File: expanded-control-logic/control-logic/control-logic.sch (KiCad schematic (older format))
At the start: 43 parts

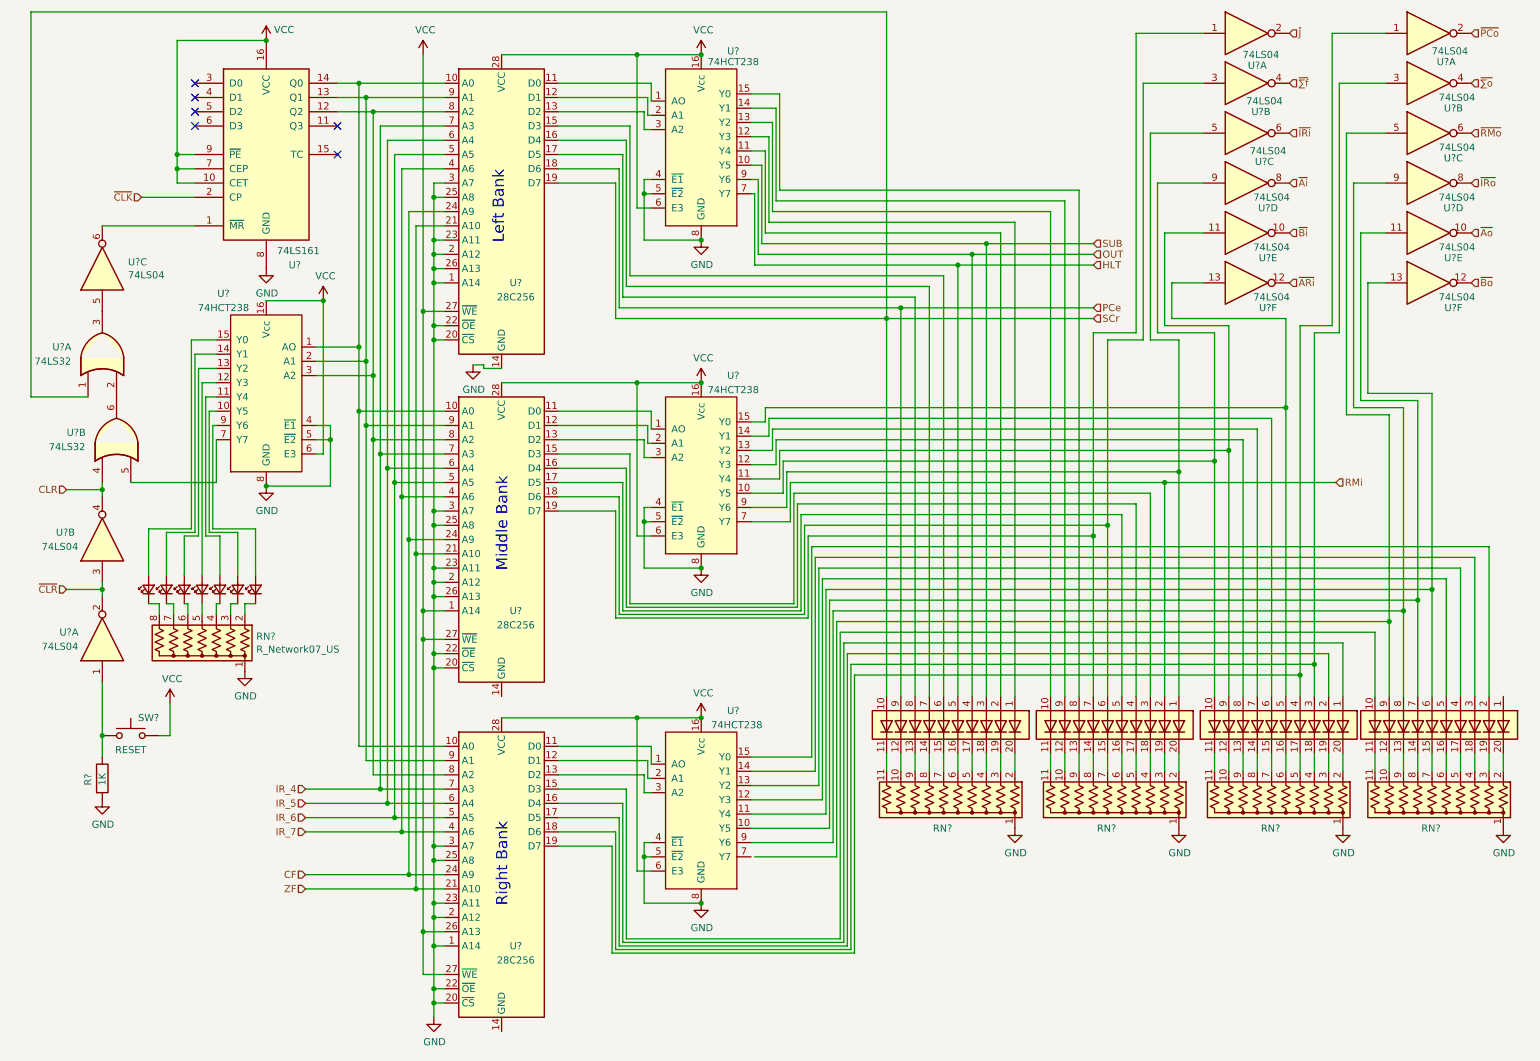
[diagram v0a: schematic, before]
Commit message: fixed werror where Y0 on 74HCT238 cannot be used for control lines
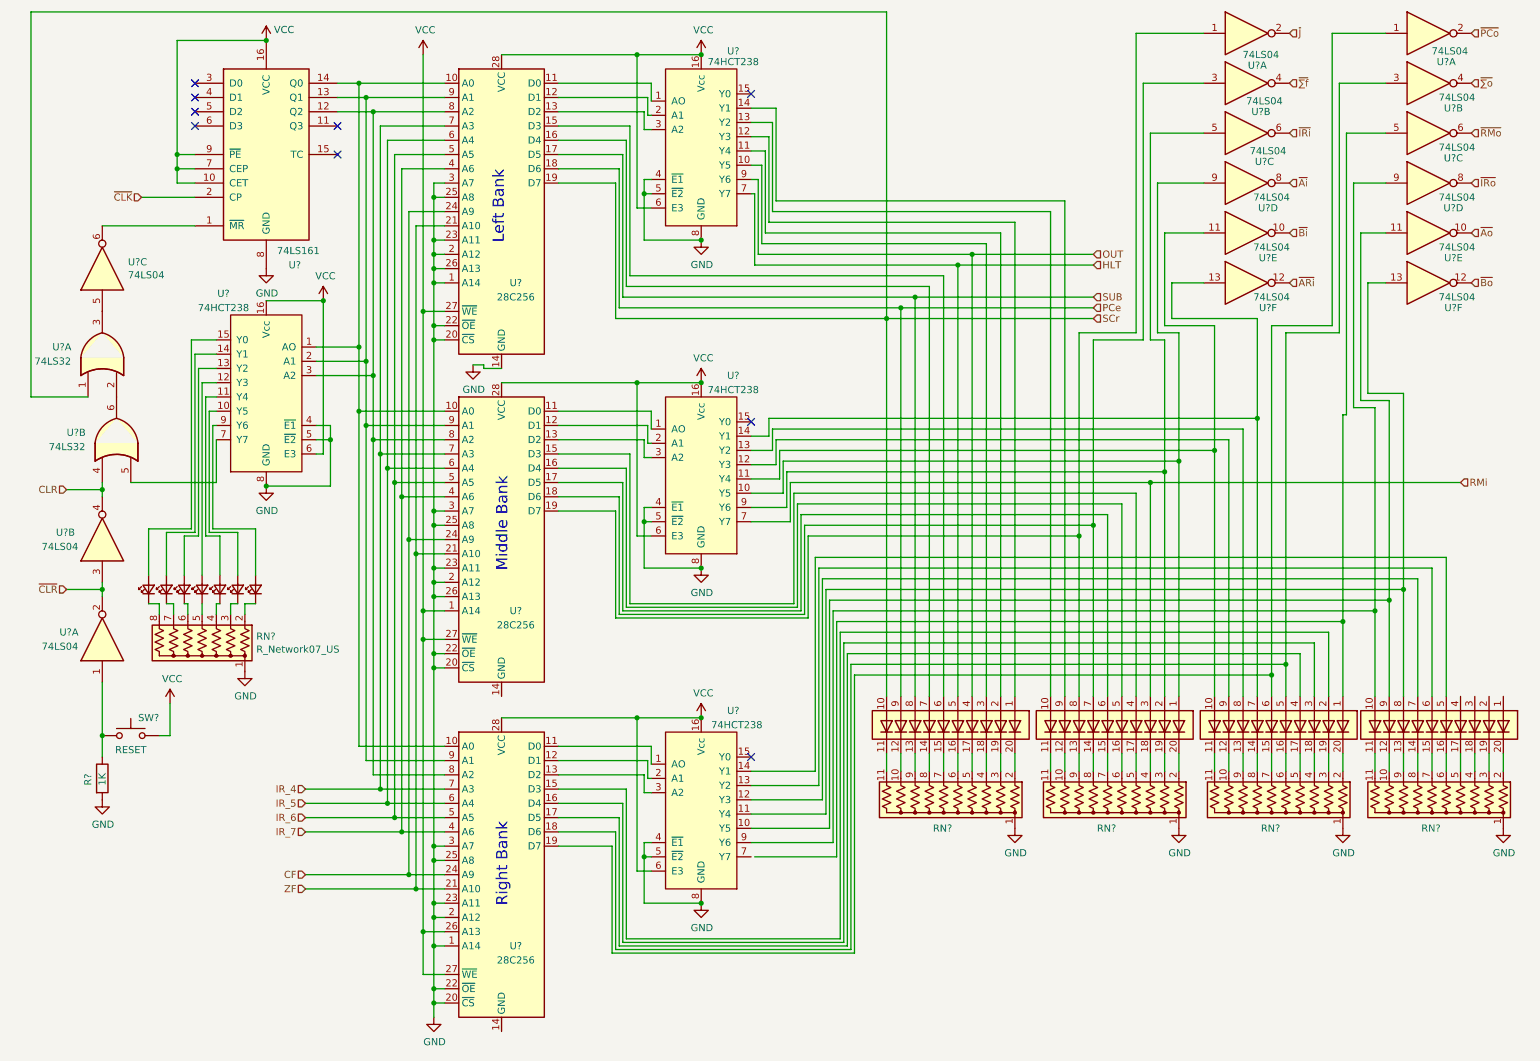
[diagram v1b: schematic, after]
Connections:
- net RMi: now also BAR?.3 (A); no longer BAR?.2 (A)
- net SUB: now also BAR?.8 (A), U?.17 (D5); no longer BAR?.3 (A), U?.10 (Y5)
- net at U?.15 (D3): now also BAR?.4 (A); no longer BAR?.3 (A)
- net at U?.16 (D4): now also BAR?.5 (A); no longer BAR?.4 (A)
- net at U?.17 (D5): now also BAR?.6 (A); no longer BAR?.5 (A)
- net at U?.18 (D6), U?.3: now also BAR?.7 (A); no longer BAR?.6 (A)
- net at U?.1, U?.19 (D7): now also BAR?.8 (A); no longer BAR?.7 (A)
- net at U?.15 (D3): now also BAR?.2 (A); no longer BAR?.10 (A)
- net at U?.16 (D4): now also BAR?.3 (A); no longer BAR?.1 (A)
- net at U?.17 (D5): now also BAR?.4 (A); no longer BAR?.2 (A)
- net at U?.18 (D6), U?.3: now also BAR?.5 (A); no longer BAR?.3 (A)
- net at U?.1, U?.19 (D7): now also BAR?.6 (A); no longer BAR?.4 (A)
- net at U?.15 (Y0): no longer BAR?.8 (A)
- net at U?.10 (Y5), U?.9: now also BAR?.1 (A); no longer BAR?.10 (A)
- net at U?.11, U?.11 (Y4): now also BAR?.10 (A); no longer BAR?.9 (A)
- net at U?.12 (Y3): now also BAR?.9 (A); no longer BAR?.8 (A)
- net at U?.13 (Y2): now also BAR?.8 (A); no longer BAR?.7 (A)
- net at U?.14 (Y1): now also BAR?.7 (A), U?.13; no longer BAR?.6 (A)
- net at U?.5, U?.9 (Y6): now also BAR?.2 (A); no longer BAR?.1 (A)
- net at U?.10 (Y5), U?.11: now also BAR?.9 (A); no longer BAR?.7 (A)
- net at U?.11 (Y4), U?.13: now also BAR?.8 (A); no longer BAR?.6 (A)
- net at U?.12 (Y3): now also BAR?.7 (A); no longer BAR?.5 (A)
- net at U?.13 (Y2): now also BAR?.6 (A); no longer BAR?.4 (A)
- net at U?.14 (Y1): now also BAR?.5 (A); no longer BAR?.3 (A)
- net at U?.15 (Y0): no longer BAR?.2 (A)
- net at U?.9, U?.9 (Y6): now also BAR?.10 (A); no longer BAR?.8 (A)
- net at U?.5: now also BAR?.1 (A); no longer BAR?.9 (A)
- new net: BAR?.3 (A), U?.10 (Y5)
- now unconnected: U?.15 (Y0)
- no-connect marks 6 -> 9
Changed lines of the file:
@@
 Text HLabel 10625 1025 2    50   Input ~ 0
 ~∑o
-Text HLabel 7975 2150 2    50   Input ~ 0
+Text HLabel 7975 2525 2    50   Input ~ 0
 SUB
 Text HLabel 9350 2075 2    50   Input ~ 0
@@
 	4225 1725 4625 1725
 Wire Wire Line
-	5575 3400 5675 3400
-Wire Wire Line
 	5575 3500 5700 3500
 Wire Wire Line
@@
 	4625 4775 5975 4775
 Wire Wire Line
-	5575 5750 6000 5750
-Wire Wire Line
 	5575 5850 6025 5850
 Wire Wire Line
@@
 Wire Wire Line
 	5575 1200 5750 1200
-Wire Wire Line
-	5575 1100 5775 1100
 $Comp
 L LED:HDSP-4840_2 BAR?
@@
 	5750 1200 5750 1850
 Wire Wire Line
-	5775 1775 7875 1775
-Wire Wire Line
-	7875 1775 7875 5325
-Wire Wire Line
-	5775 1100 5775 1775
-Wire Wire Line
-	5675 3400 5675 3300
-Wire Wire Line
 	5725 3600 5725 3450
 Wire Wire Line
@@
 	5975 4775 5975 4200
 Wire Wire Line
-	6000 5750 6000 4275
-Wire Wire Line
 	6025 5850 6025 4350
 Wire Wire Line
-	10750 5325 10750 4275
-Wire Wire Line
 	6050 5950 6050 4425
 Wire Wire Line
@@
 	6300 7125 6300 5175
 Wire Wire Line
-	6300 5175 9425 5175
-Wire Wire Line
-	9425 5175 9425 5325
-Wire Wire Line
-	9525 5100 6275 5100
-Wire Wire Line
-	9525 5100 9525 5325
+	6300 5175 9225 5175
 Wire Wire Line
 	6275 5100 6275 7100
 Wire Wire Line
-	9625 5025 6250 5025
-Wire Wire Line
-	9625 5025 9625 5325
-Wire Wire Line
 	6250 5025 6250 7075
 Wire Wire Line
-	9725 4950 6225 4950
-Wire Wire Line
-	9725 4950 9725 5325
-Wire Wire Line
-	9950 4875 6200 4875
-Wire Wire Line
-	9950 4875 9950 5325
-Wire Wire Line
-	10050 4800 6175 4800
-Wire Wire Line
-	10050 4800 10050 5325
-Wire Wire Line
-	10150 4725 6150 4725
-Wire Wire Line
-	10150 4725 10150 5325
-Wire Wire Line
-	10250 4650 6125 4650
-Wire Wire Line
-	10250 4650 10250 5325
-Wire Wire Line
-	10350 4575 6100 4575
-Wire Wire Line
-	10350 4575 10350 5325
-Wire Wire Line
-	10450 4500 6075 4500
-Wire Wire Line
-	10450 4500 10450 5325
-Wire Wire Line
-	10550 4425 6050 4425
-Wire Wire Line
-	10550 4425 10550 5325
-Wire Wire Line
-	10650 4350 6025 4350
-Wire Wire Line
-	10650 4350 10650 5325
-Wire Wire Line
-	10750 4275 6000 4275
-Wire Wire Line
-	7975 4200 5975 4200
-Wire Wire Line
-	7975 4200 7975 5325
-Wire Wire Line
-	5950 4125 8075 4125
-Wire Wire Line
-	8075 4125 8075 5325
-Wire Wire Line
-	8175 4050 5925 4050
-Wire Wire Line
-	8175 4050 8175 5325
-Wire Wire Line
-	8275 3975 5900 3975
-Wire Wire Line
-	8275 3975 8275 5325
-Wire Wire Line
-	8375 3900 5875 3900
-Wire Wire Line
-	8375 3900 8375 5325
-Wire Wire Line
-	8475 3825 5850 3825
-Wire Wire Line
-	8475 3825 8475 5325
-Wire Wire Line
-	8575 3750 5825 3750
-Wire Wire Line
-	8575 3750 8575 5325
-Wire Wire Line
-	8825 3675 5800 3675
-Wire Wire Line
-	8825 3675 8825 5325
-Wire Wire Line
-	8925 3600 5775 3600
-Wire Wire Line
-	8925 3600 8925 5325
-Wire Wire Line
-	9025 3525 5750 3525
-Wire Wire Line
-	9025 3525 9025 5325
-Wire Wire Line
-	9125 3450 5725 3450
-Wire Wire Line
-	9125 3450 9125 5325
-Wire Wire Line
-	9225 3375 5700 3375
-Wire Wire Line
-	9225 3375 9225 5325
+	5950 4125 7975 4125
 Wire Wire Line
 	5700 3375 5700 3500
-Wire Wire Line
-	9325 3300 5675 3300
-Wire Wire Line
-	9325 3300 9325 5325
 Wire Wire Line
 	6525 2675 6525 525
@@
 Connection ~ 7125 2225
 Wire Wire Line
-	7225 2150 7975 2150
-Connection ~ 7225 2150
-Wire Wire Line
 	6525 2675 7975 2675
 Wire Wire Line
-	7975 4200 7975 2775
-Wire Wire Line
-	7975 2775 8275 2775
-Wire Wire Line
 	8275 2775 8275 675
 Wire Wire Line
 	8275 675  8750 675
-Connection ~ 7975 4200
-Wire Wire Line
-	8075 4125 8075 2825
-Wire Wire Line
-	8075 2825 8325 2825
 Wire Wire Line
 	8325 2825 8325 1025
 Wire Wire Line
 	8325 1025 8750 1025
-Connection ~ 8075 4125
-Wire Wire Line
-	9425 5175 9425 2725
-Wire Wire Line
-	9425 2725 9650 2725
-Connection ~ 9425 5175
-Wire Wire Line
-	9525 5100 9525 2775
-Wire Wire Line
-	9525 2775 9700 2775
-Connection ~ 9525 5100
 $Comp
 L 74xx:74LS04 U?
@@
 	1    0    0    -1
 $EndComp
-Text HLabel 9675 3825 2    50   Input ~ 0
+Text HLabel 10550 3825 2    50   Input ~ 0
 RMi
 Wire Wire Line
-	8475 3825 9675 3825
-Connection ~ 8475 3825
-Wire Wire Line
-	8575 3750 8575 2825
-Wire Wire Line
-	8575 2825 8375 2825
-Wire Wire Line
 	8375 2825 8375 1375
 Wire Wire Line
 	8375 1375 8750 1375
-Connection ~ 8575 3750
-Wire Wire Line
-	8825 3675 8825 2775
-Wire Wire Line
-	8825 2775 8425 2775
 Wire Wire Line
 	8425 2775 8425 1725
 Wire Wire Line
 	8425 1725 8750 1725
-Connection ~ 8825 3675
-Wire Wire Line
-	8925 3600 8925 2725
-Wire Wire Line
-	8925 2725 8475 2725
 Wire Wire Line
 	8475 2725 8475 2075
 Wire Wire Line
 	8475 2075 8750 2075
-Connection ~ 8925 3600
-Wire Wire Line
-	9325 3300 9325 2675
-Wire Wire Line
-	9325 2675 8525 2675
 Wire Wire Line
 	8525 2675 8525 2425
 Wire Wire Line
 	8525 2425 8750 2425
-Connection ~ 9325 3300
 Wire Wire Line
 	9650 675  10025 675
@@
 	9700 1025 9700 2775
 Wire Wire Line
-	10050 4800 10050 3350
-Wire Wire Line
-	10050 3350 9750 3350
-Wire Wire Line
 	9750 3350 9750 1375
 Wire Wire Line
 	9750 1375 10025 1375
-Connection ~ 10050 4800
-Wire Wire Line
-	10150 4725 10150 3300
-Wire Wire Line
-	10150 3300 9800 3300
 Wire Wire Line
 	9800 3300 9800 1725
 Wire Wire Line
 	9800 1725 10025 1725
-Connection ~ 10150 4725
-Wire Wire Line
-	10250 4650 10250 3250
-Wire Wire Line
-	10250 3250 9850 3250
 Wire Wire Line
 	9850 3250 9850 2075
 Wire Wire Line
 	9850 2075 10025 2075
-Connection ~ 10250 4650
-Wire Wire Line
-	10350 4575 10350 3200
-Wire Wire Line
-	10350 3200 9900 3200
 Wire Wire Line
 	9900 3200 9900 2425
 Wire Wire Line
 	9900 2425 10025 2425
-Connection ~ 10350 4575
+Wire Wire Line
+	6725 2525 7975 2525
+Connection ~ 6725 2525
+NoConn ~ 5575 1100
+NoConn ~ 5575 3400
+NoConn ~ 5575 5750
+Wire Wire Line
+	7875 5325 7875 4200
+Wire Wire Line
+	7875 4200 5975 4200
+Wire Wire Line
+	7875 4200 7875 2775
+Wire Wire Line
+	7875 2775 8275 2775
+Connection ~ 7875 4200
+Wire Wire Line
+	7975 5325 7975 4125
+Wire Wire Line
+	7975 4125 7975 2825
+Wire Wire Line
+	7975 2825 8325 2825
+Connection ~ 7975 4125
+Wire Wire Line
+	8075 5325 8075 4050
+Wire Wire Line
+	8075 4050 5925 4050
+Wire Wire Line
+	8175 5325 8175 3975
+Wire Wire Line
+	8175 3975 5900 3975
+Wire Wire Line
+	8275 5325 8275 3900
+Wire Wire Line
+	8275 3900 5875 3900
+Wire Wire Line
+	5850 3825 8375 3825
+Wire Wire Line
+	8375 5325 8375 3825
+Wire Wire Line
+	8475 5325 8475 3750
+Connection ~ 8475 3750
+Wire Wire Line
+	8475 3750 5825 3750
+Wire Wire Line
+	8475 3750 8475 2825
+Wire Wire Line
+	8475 2825 8375 2825
+Wire Wire Line
+	8575 5325 8575 3675
+Wire Wire Line
+	8575 3675 5800 3675
+Wire Wire Line
+	8575 2775 8425 2775
+Wire Wire Line
+	8575 2775 8575 3675
+Connection ~ 8575 3675
+Wire Wire Line
+	8825 5325 8825 3600
+Connection ~ 8825 3600
+Wire Wire Line
+	8825 3600 5775 3600
+Wire Wire Line
+	8825 3600 8825 2725
+Wire Wire Line
+	8825 2725 8475 2725
+Wire Wire Line
+	8925 5325 8925 3525
+Wire Wire Line
+	8925 3525 5750 3525
+Wire Wire Line
+	9025 5325 9025 3450
+Wire Wire Line
+	9025 3450 5725 3450
+Wire Wire Line
+	9125 5325 9125 3375
+Connection ~ 9125 3375
+Wire Wire Line
+	9125 3375 5700 3375
+Wire Wire Line
+	9125 3375 9125 2675
+Wire Wire Line
+	9125 2675 8525 2675
+Wire Wire Line
+	9225 5325 9225 5175
+Connection ~ 9225 5175
+Wire Wire Line
+	9225 5175 9225 2725
+Wire Wire Line
+	9225 2725 9650 2725
+Wire Wire Line
+	9325 5325 9325 5100
+Connection ~ 9325 5100
+Wire Wire Line
+	9325 5100 6275 5100
+Wire Wire Line
+	9325 5100 9325 2775
+Wire Wire Line
+	9325 2775 9700 2775
+Wire Wire Line
+	9425 5325 9425 5025
+Wire Wire Line
+	9425 5025 6250 5025
+Wire Wire Line
+	9525 5325 9525 4950
+Wire Wire Line
+	9525 4950 6225 4950
+Wire Wire Line
+	9625 5325 9625 4875
+Wire Wire Line
+	9625 4875 6200 4875
+Wire Wire Line
+	9725 5325 9725 4800
+Connection ~ 9725 4800
+Wire Wire Line
+	9725 4800 6175 4800
+Wire Wire Line
+	9725 4800 9725 3350
+Wire Wire Line
+	9725 3350 9750 3350
+Wire Wire Line
+	8375 3825 10550 3825
+Connection ~ 8375 3825
+Wire Wire Line
+	9950 5325 9950 4725
+Connection ~ 9950 4725
+Wire Wire Line
+	9950 4725 6150 4725
+Wire Wire Line
+	9950 4725 9950 3300
+Wire Wire Line
+	9950 3300 9800 3300
+Wire Wire Line
+	10050 5325 10050 4650
+Connection ~ 10050 4650
+Wire Wire Line
+	10050 4650 6125 4650
+Wire Wire Line
+	10050 4650 10050 3250
+Wire Wire Line
+	10050 3250 9850 3250
+Wire Wire Line
+	10150 5325 10150 4575
+Connection ~ 10150 4575
+Wire Wire Line
+	10150 4575 6100 4575
+Wire Wire Line
+	10150 4575 10150 3200
+Wire Wire Line
+	10150 3200 9900 3200
+Wire Wire Line
+	10250 5325 10250 4500
+Wire Wire Line
+	10250 4500 6075 4500
+Wire Wire Line
+	10350 5325 10350 4425
+Wire Wire Line
+	10350 4425 6050 4425
+Wire Wire Line
+	10450 5325 10450 4350
+Wire Wire Line
+	10450 4350 6025 4350
 $EndSCHEMATC

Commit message: addressed some design bugs
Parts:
- removed RN?: R_Network07_US, Resistor_THT:R_Array_SIP8, symbol Device:R_Network07_US
- added D?: LED_Small, symbol Device:LED_Small
- added RN?: R_Network08_US, Resistor_THT:R_Array_SIP9, symbol Device:R_Network08_US
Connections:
- net GND: now also RN?.1 (common)
- net ~ARi: now also U?.8; no longer U?.12
- net ~Ai: now also U?.12; no longer U?.8
- net at BAR?.1 (A), U?.10 (Y5): now also U?.13; no longer U?.9
- net at BAR?.7 (A), U?.14 (Y1): now also U?.9; no longer U?.13
- net at U?.7 (Y7): now also BAR?.1 (A), U?.5
- net at U?.11 (Q3): now also U?.5
- net at U?.7 (Y7): now also D?.2 (A); no longer U?.5
- net at D?.1 (K): now also RN?.9 (R8)
- net at D?.1 (K): now also RN?.8 (R7)
- net at D?.1 (K): now also RN?.7 (R6)
- net at D?.1 (K): now also RN?.6 (R5)
- net at D?.1 (K): now also RN?.5 (R4)
- net at D?.1 (K): now also RN?.4 (R3)
- net at D?.1 (K): now also RN?.3 (R2)
- new net: D?.1 (K), RN?.2 (R1)
- no-connect marks 9 -> 8
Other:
- moved on the sheet: U?D, U?F
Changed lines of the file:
@@
 encoding utf-8
 Sheet 1 1
-Title ""
+Title "Eater SAP-1 Expanded Control Logic"
 Date ""
 Rev ""
@@
 	5575 6350 6150 6350
 Wire Wire Line
-	5600 6450 6175 6450
-Wire Wire Line
 	4225 5975 4700 5975
 Wire Wire Line
@@
 	2675 1225 2925 1225
 Connection ~ 2925 1225
-NoConn ~ 2675 1325
 NoConn ~ 2675 1525
 $Comp
@@
 Connection ~ 2575 2550
 Wire Wire Line
-	1825 3525 1825 3825
-Wire Wire Line
-	1825 3825 1225 3825
-Wire Wire Line
 	1550 1525 1550 725
 Wire Wire Line
@@
 	1    0    0    -1
 $EndComp
-$Comp
-L Device:R_Network07_US RN?
-U 1 1 627DCA1B
-P 1725 4950
-F 0 "RN?" H 1345 4904 50  0000 R CNN
-F 1 "R_Network07_US" H 1345 4995 50  0000 R CNN
-F 2 "Resistor_THT:R_Array_SIP8" V 2200 4950 50  0001 C CNN
-F 3 "http://www.vishay.com/docs/31509/csc.pdf" H 1725 4950 50  0001 C CNN
-	1    1725 4950
-	-1   0    0    1
-$EndComp
 Wire Wire Line
 	1350 4150 1350 4475
@@
 L power:GND #PWR?
 U 1 1 6325A30E
-P 2025 5150
-F 0 "#PWR?" H 2025 4900 50  0001 C CNN
-F 1 "GND" H 2030 4977 50  0000 C CNN
-F 2 "" H 2025 5150 50  0001 C CNN
-F 3 "" H 2025 5150 50  0001 C CNN
-	1    2025 5150
+P 2125 5150
+F 0 "#PWR?" H 2125 4900 50  0001 C CNN
+F 1 "GND" H 2130 4977 50  0000 C CNN
+F 2 "" H 2125 5150 50  0001 C CNN
+F 3 "" H 2125 5150 50  0001 C CNN
+	1    2125 5150
 	1    0    0    -1
 $EndComp
@@
 L 74xx:74LS04 U?
 U 4 1 63AF0D4E
-P 9050 1725
-F 0 "U?" H 9200 1550 50  0000 C CNN
-F 1 "74LS04" H 9225 1625 50  0000 C CNN
-F 2 "" H 9050 1725 50  0001 C CNN
-F 3 "http://www.ti.com/lit/gpn/sn74LS04" H 9050 1725 50  0001 C CNN
-	4    9050 1725
+P 9050 2425
+F 0 "U?" H 9200 2250 50  0000 C CNN
+F 1 "74LS04" H 9225 2325 50  0000 C CNN
+F 2 "" H 9050 2425 50  0001 C CNN
+F 3 "http://www.ti.com/lit/gpn/sn74LS04" H 9050 2425 50  0001 C CNN
+	4    9050 2425
 	1    0    0    -1
 $EndComp
@@
 L 74xx:74LS04 U?
 U 6 1 63DC8B63
-P 9050 2425
-F 0 "U?" H 9200 2250 50  0000 C CNN
-F 1 "74LS04" H 9225 2325 50  0000 C CNN
-F 2 "" H 9050 2425 50  0001 C CNN
-F 3 "http://www.ti.com/lit/gpn/sn74LS04" H 9050 2425 50  0001 C CNN
-	6    9050 2425
+P 9050 1725
+F 0 "U?" H 9200 1550 50  0000 C CNN
+F 1 "74LS04" H 9225 1625 50  0000 C CNN
+F 2 "" H 9050 1725 50  0001 C CNN
+F 3 "http://www.ti.com/lit/gpn/sn74LS04" H 9050 1725 50  0001 C CNN
+	6    9050 1725
 	1    0    0    -1
 $EndComp
@@
 Wire Wire Line
 	10450 4350 6025 4350
+$Comp
+L Device:LED_Small D?
+U 1 1 5FF03B5B
+P 2225 4575
+F 0 "D?" V 2225 4505 50  0001 R CNN
+F 1 "LED_Small" V 2180 4505 50  0001 R CNN
+F 2 "" V 2225 4575 50  0001 C CNN
+F 3 "~" V 2225 4575 50  0001 C CNN
+	1    2225 4575
+	0    -1   -1   0
+$EndComp
+Wire Wire Line
+	1825 4125 2225 4125
+Wire Wire Line
+	2225 4125 2225 4475
+Wire Wire Line
+	1825 3525 1825 4125
+Wire Wire Line
+	2675 1325 2750 1325
+Wire Wire Line
+	2750 1325 2750 575
+Wire Wire Line
+	2750 575  1450 575
+Wire Wire Line
+	1450 575  1450 3825
+Wire Wire Line
+	1450 3825 1225 3825
+$Comp
+L Device:R_Network08_US RN?
+U 1 1 6011EC35
+P 1725 4950
+F 0 "RN?" H 1245 4904 50  0000 R CNN
+F 1 "R_Network08_US" H 1245 4995 50  0000 R CNN
+F 2 "Resistor_THT:R_Array_SIP9" V 2200 4950 50  0001 C CNN
+F 3 "http://www.vishay.com/docs/31509/csc.pdf" H 1725 4950 50  0001 C CNN
+	1    1725 4950
+	-1   0    0    1
+$EndComp
+Wire Wire Line
+	2225 4675 2125 4675
+Wire Wire Line
+	2125 4675 2125 4750
+Wire Wire Line
+	5575 6450 6175 6450
 $EndSCHEMATC

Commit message: improve documentation
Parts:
- gave numbers to parts that had none: 31
